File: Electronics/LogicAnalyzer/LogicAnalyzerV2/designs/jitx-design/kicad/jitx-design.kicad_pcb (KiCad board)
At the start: 4 copper layers, 55.5 x 65 mm, 103 parts

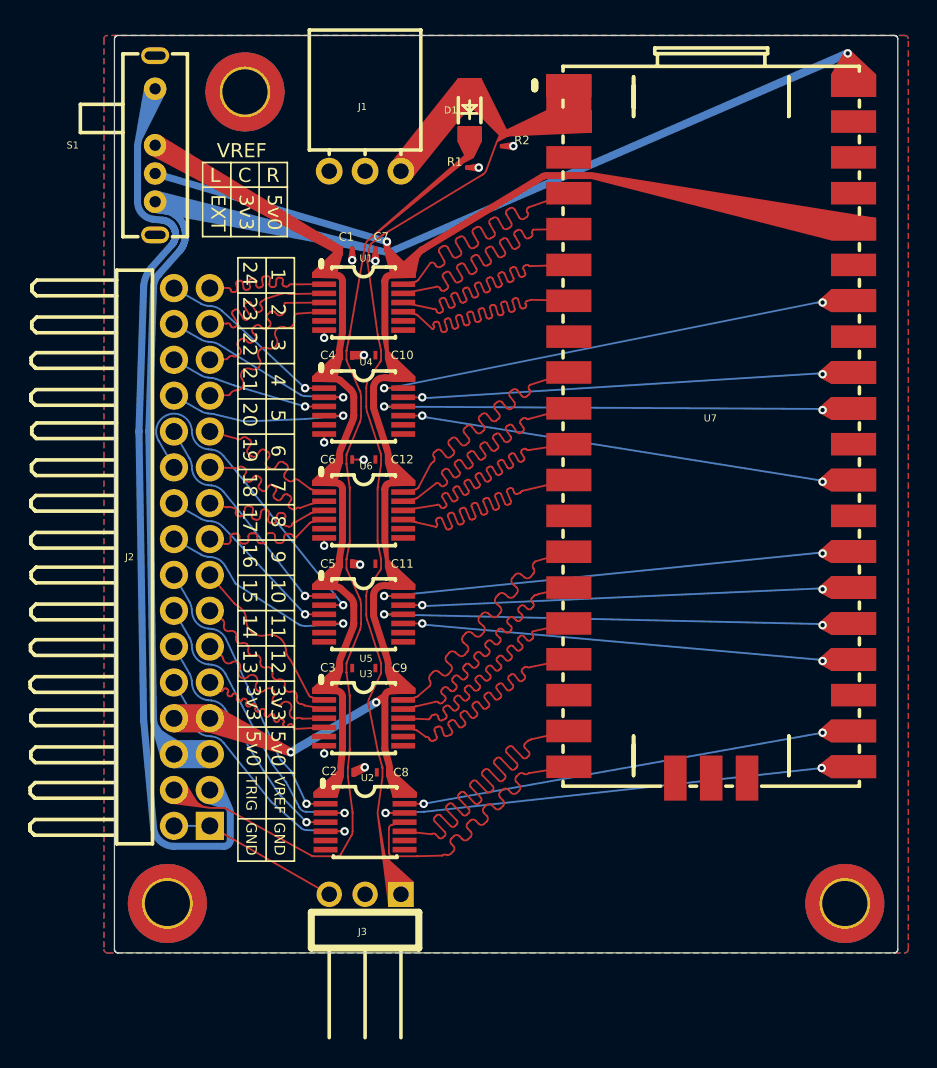
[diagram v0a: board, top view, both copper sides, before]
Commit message: Pico 2 working with new PCB design
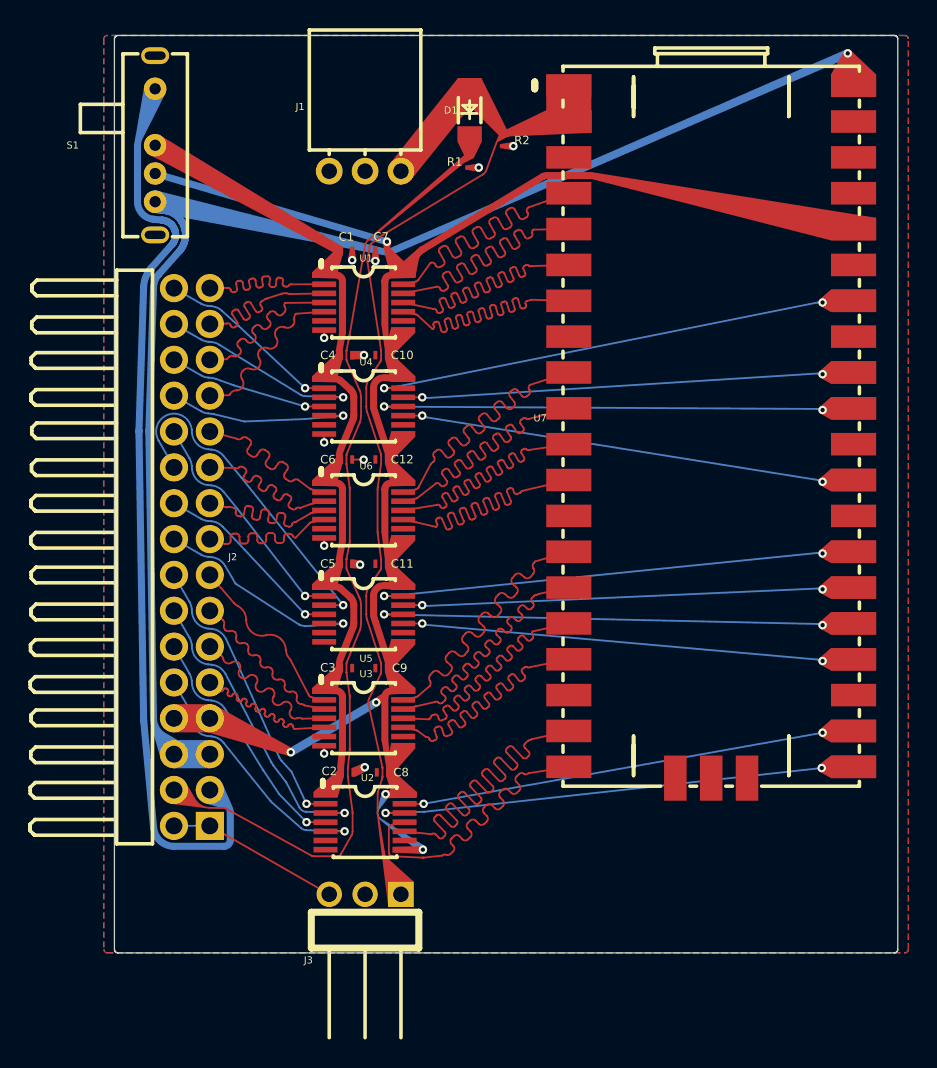
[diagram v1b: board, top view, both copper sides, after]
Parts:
- removed ?: , jitx-design:dummy17
- removed ?: , jitx-design:dummy26
- removed ?: , jitx-design:dummy21
- removed ?: , jitx-design:dummy10
- removed ?: , jitx-design:dummy16
- removed ?: , jitx-design:dummy40
- removed ?: , jitx-design:dummy60
- removed ?: , jitx-design:dummy29
- removed ?: , jitx-design:dummy36
- removed ?: , jitx-design:dummy42
- removed ?: , jitx-design:dummy49
- removed ?: , jitx-design:dummy62
- removed ?: , jitx-design:dummy11
- removed ?: , jitx-design:dummy68
- removed ?: , jitx-design:dummy32
- removed ?: , jitx-design:dummy34
- removed ?: , jitx-design:dummy55
- removed ?: , jitx-design:dummy0
- removed ?: , jitx-design:dummy23
- removed ?: , jitx-design:dummy18
- removed ?: , jitx-design:dummy27
- removed ?: , jitx-design:dummy6
- removed ?: , jitx-design:dummy54
- removed ?: , jitx-design:dummy30
- removed ?: , jitx-design:dummy44
- removed ?: , jitx-design:dummy63
- removed ?: , jitx-design:dummy35
- removed ?: , jitx-design:dummy58
- removed ?: , jitx-design:dummy7
- removed ?: , jitx-design:dummy15
- removed ?: , jitx-design:dummy5
- removed ?: , jitx-design:dummy45
- removed ?: , jitx-design:dummy3
- removed ?: , jitx-design:dummy53
- removed ?: , jitx-design:dummy19
- removed ?: , jitx-design:dummy70
- removed ?: , jitx-design:dummy2
- removed ?: , jitx-design:dummy28
- removed ?: , jitx-design:dummy37
- removed ?: , jitx-design:dummy69
- removed ?: , jitx-design:dummy50
- removed ?: , jitx-design:dummy38
- removed ?: , jitx-design:dummy71
- removed ?: , jitx-design:dummy57
- removed ?: , jitx-design:dummy8
- removed ?: , jitx-design:dummy65
- removed ?: , jitx-design:dummy25
- removed ?: , jitx-design:dummy67
- removed ?: , jitx-design:dummy48
- removed ?: , jitx-design:dummy1
- removed ?: , jitx-design:dummy4
- removed ?: , jitx-design:dummy41
- removed ?: , jitx-design:dummy52
- removed ?: , jitx-design:dummy20
- removed ?: , jitx-design:dummy31
- removed ?: , jitx-design:dummy9
- removed ?: , jitx-design:dummy43
- removed ?: , jitx-design:dummy22
- removed ?: , jitx-design:dummy72
- removed ?: , jitx-design:dummy47
- removed ?: , jitx-design:dummy39
- removed ?: , jitx-design:dummy12
- removed ?: , jitx-design:dummy61
- removed ?: , jitx-design:dummy46
- removed ?: , jitx-design:dummy56
- removed ?: , jitx-design:dummy66
- removed ?: , jitx-design:dummy59
- removed ?: , jitx-design:dummy24
- removed ?: , jitx-design:dummy14
- removed ?: , jitx-design:dummy51
- removed ?: , jitx-design:dummy33
- removed ?: , jitx-design:dummy13
- removed ?: , jitx-design:dummy64
- removed G***: LOGO, Logo:sembei_scale_small
- removed MH1, MH2, MH3: MountingHole_3.2mm_M3_DIN965_Pad_TopBottom, MountingHole:MountingHole_3.2mm_M3_DIN965_Pad_TopBottom
- C1: footprint jitx-design:Pkg0402_6 -> jitx-design:Pkg0402_13
- C10: footprint jitx-design:Pkg0402 -> jitx-design:Pkg0402_7
- C11: footprint jitx-design:Pkg0402_4 -> jitx-design:Pkg0402_11
- C12: footprint jitx-design:Pkg0402_2 -> jitx-design:Pkg0402_9
- C2: footprint jitx-design:Pkg0402_3 -> jitx-design:Pkg0402_10
- C3: footprint jitx-design:Pkg0402_1 -> jitx-design:Pkg0402_8
- C4: footprint jitx-design:Pkg0402_8 -> jitx-design:Pkg0402_2
- C5: footprint jitx-design:Pkg0402_10 -> jitx-design:Pkg0402_3
- C6: footprint jitx-design:Pkg0402_12 -> jitx-design:Pkg0402_5
- C7: footprint jitx-design:Pkg0402_7 -> jitx-design:Pkg0402_1
- C8: footprint jitx-design:Pkg0402_11 -> jitx-design:Pkg0402_4
- C9: footprint jitx-design:Pkg0402_13 -> jitx-design:Pkg0402_6
- R1: footprint jitx-design:Pkg0402_9 -> jitx-design:Pkg0402
- R2: footprint jitx-design:Pkg0402_5 -> jitx-design:Pkg0402_12
- U1: footprint jitx-design:TSSOP_14_L5_0_W4_4_P0_65_LS6_4_BL_1 -> jitx-design:TSSOP_14_L5_0_W4_4_P0_65_LS6_4_BL_3
- U2: footprint jitx-design:TSSOP_14_L5_0_W4_4_P0_65_LS6_4_BL -> jitx-design:TSSOP_14_L5_0_W4_4_P0_65_LS6_4_BL_2
- U3: footprint jitx-design:TSSOP_14_L5_0_W4_4_P0_65_LS6_4_BL_2 -> jitx-design:TSSOP_14_L5_0_W4_4_P0_65_LS6_4_BL_4
- U4: footprint jitx-design:TSSOP_14_L5_0_W4_4_P0_65_LS6_4_BL_5 -> jitx-design:TSSOP_14_L5_0_W4_4_P0_65_LS6_4_BL_1
- U5: footprint jitx-design:TSSOP_14_L5_0_W4_4_P0_65_LS6_4_BL_3 -> jitx-design:TSSOP_14_L5_0_W4_4_P0_65_LS6_4_BL_5
- U6: footprint jitx-design:TSSOP_14_L5_0_W4_4_P0_65_LS6_4_BL_4 -> jitx-design:TSSOP_14_L5_0_W4_4_P0_65_LS6_4_BL
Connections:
- U1 pad 8: (no net) -> POWER_3v3
- U2 pad 8: (no net) -> POWER_3v3
- U3 pad 8: (no net) -> POWER_3v3
- U4 pad 8: (no net) -> POWER_3v3
- U5 pad 8: (no net) -> POWER_3v3
- U6 pad 8: (no net) -> POWER_3v3
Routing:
- net POWER_3v3: track 44.7 -> 43.0 mm, vias 3 -> 5
- net EXT_CHAIN: track 48.8 -> 50.1 mm
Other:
- board text removed: "1"
- board text removed: "10"
- board text removed: "11"
- board text removed: "12"
- board text removed: "13"
- board text removed: "14"
- board text removed: "15"
- board text removed: "16"
- board text removed: "17"
- board text removed: "18"
- board text removed: "19"
- board text removed: "2"
- board text removed: "20"
- board text removed: "21"
- board text removed: "22"
- board text removed: "23"
- board text removed: "24"
- board text removed: "3"
- board text removed: "3v3"
- board text removed: "4"
- board text removed: "5"
- board text removed: "5v0"
- board text removed: "6"
- board text removed: "7"
- board text removed: "8"
- board text removed: "9"
- board text removed: "By El Dr. Gusman - 2024"
- board text removed: "C"
- board text removed: "EXT"
- board text removed: "GND"
- board text removed: "L"
- board text removed: "LogicAnalyzer"
- board text removed: "R"
- board text removed: "TRIG"
- board text removed: "VREF"
- board text removed: "https://github.com/gusmanb/logicanalyzer"

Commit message: Updated gitignore
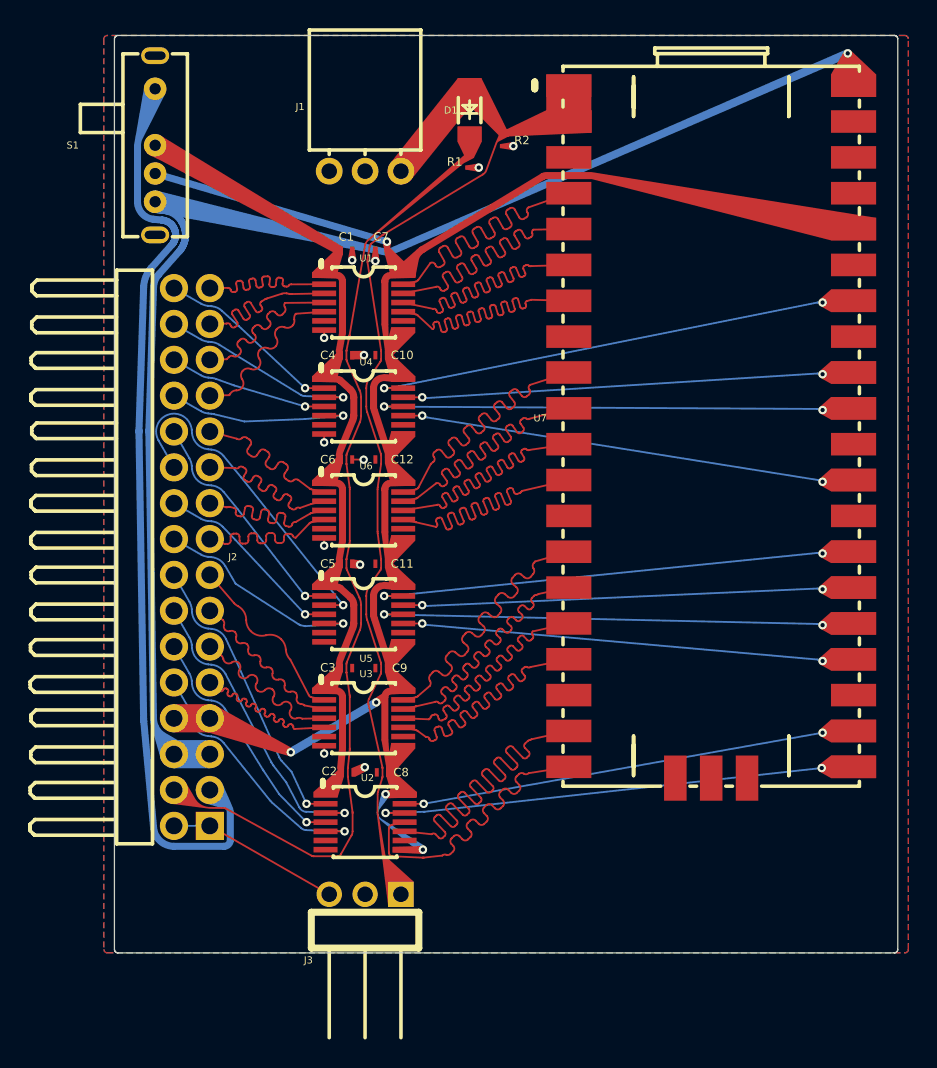
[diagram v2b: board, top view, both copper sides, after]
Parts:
- C1: footprint jitx-design:Pkg0402_13 -> jitx-design:Pkg0402_3
- C10: footprint jitx-design:Pkg0402_7 -> jitx-design:Pkg0402_11
- C11: footprint jitx-design:Pkg0402_11 -> jitx-design:Pkg0402_1
- C12: footprint jitx-design:Pkg0402_9 -> jitx-design:Pkg0402_13
- C2: footprint jitx-design:Pkg0402_10 -> jitx-design:Pkg0402
- C3: footprint jitx-design:Pkg0402_8 -> jitx-design:Pkg0402_12
- C4: footprint jitx-design:Pkg0402_2 -> jitx-design:Pkg0402_6
- C5: footprint jitx-design:Pkg0402_3 -> jitx-design:Pkg0402_7
- C6: footprint jitx-design:Pkg0402_5 -> jitx-design:Pkg0402_9
- C7: footprint jitx-design:Pkg0402_1 -> jitx-design:Pkg0402_5
- C8: footprint jitx-design:Pkg0402_4 -> jitx-design:Pkg0402_8
- C9: footprint jitx-design:Pkg0402_6 -> jitx-design:Pkg0402_10
- R1: footprint jitx-design:Pkg0402 -> jitx-design:Pkg0402_4
- R2: footprint jitx-design:Pkg0402_12 -> jitx-design:Pkg0402_2
- U1: footprint jitx-design:TSSOP_14_L5_0_W4_4_P0_65_LS6_4_BL_3 -> jitx-design:TSSOP_14_L5_0_W4_4_P0_65_LS6_4_BL_5
- U2: footprint jitx-design:TSSOP_14_L5_0_W4_4_P0_65_LS6_4_BL_2 -> jitx-design:TSSOP_14_L5_0_W4_4_P0_65_LS6_4_BL_4
- U3: footprint jitx-design:TSSOP_14_L5_0_W4_4_P0_65_LS6_4_BL_4 -> jitx-design:TSSOP_14_L5_0_W4_4_P0_65_LS6_4_BL
- U4: footprint jitx-design:TSSOP_14_L5_0_W4_4_P0_65_LS6_4_BL_1 -> jitx-design:TSSOP_14_L5_0_W4_4_P0_65_LS6_4_BL_3
- U5: footprint jitx-design:TSSOP_14_L5_0_W4_4_P0_65_LS6_4_BL_5 -> jitx-design:TSSOP_14_L5_0_W4_4_P0_65_LS6_4_BL_1
- U6: footprint jitx-design:TSSOP_14_L5_0_W4_4_P0_65_LS6_4_BL -> jitx-design:TSSOP_14_L5_0_W4_4_P0_65_LS6_4_BL_2
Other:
- net class Default added: clearance 0.2, trace_width 0.13, via_dia 0.0774192, via_drill 0.254
